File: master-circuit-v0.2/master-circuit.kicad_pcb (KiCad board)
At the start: 4 copper layers, 64 x 86 mm, 254 parts, among them U6 20nF 5%, X2 24MHz

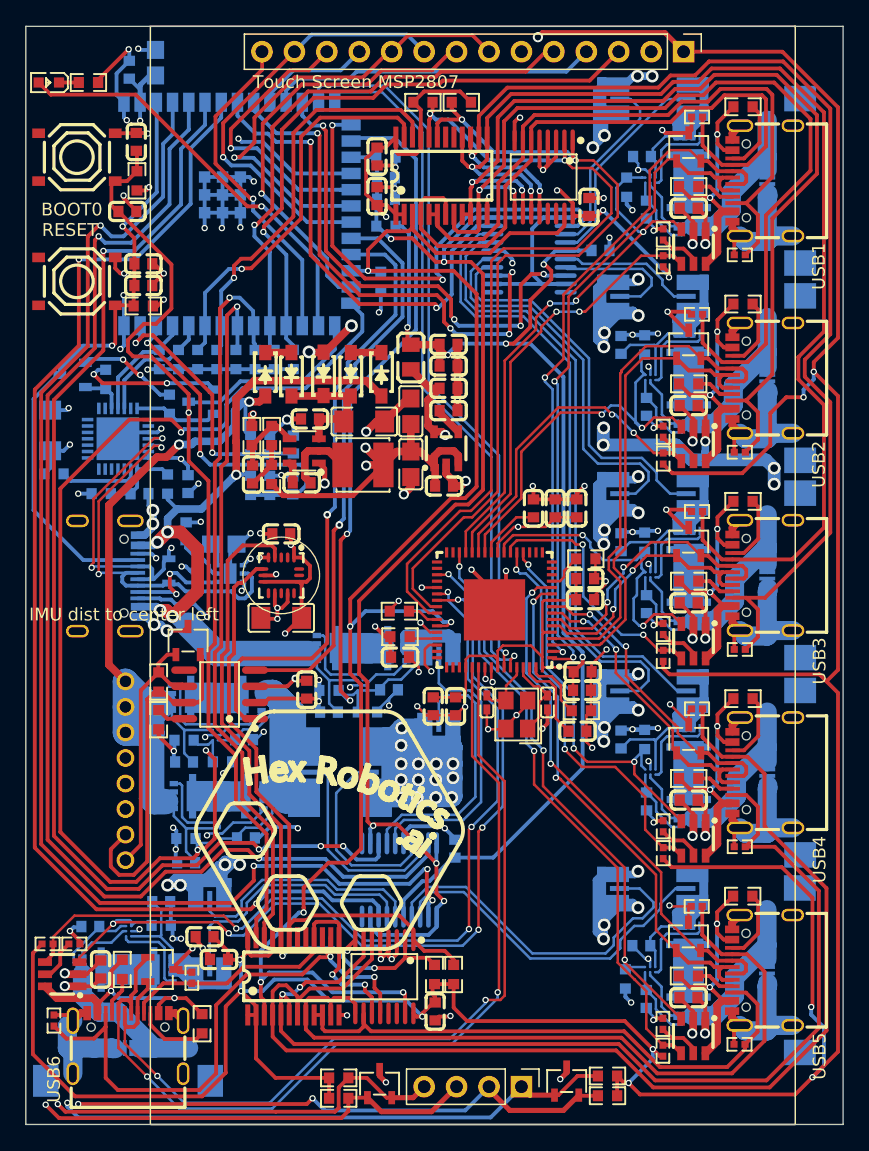
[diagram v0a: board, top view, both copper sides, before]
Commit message: Argh, some chips out of stock, got to do a slight redesign.
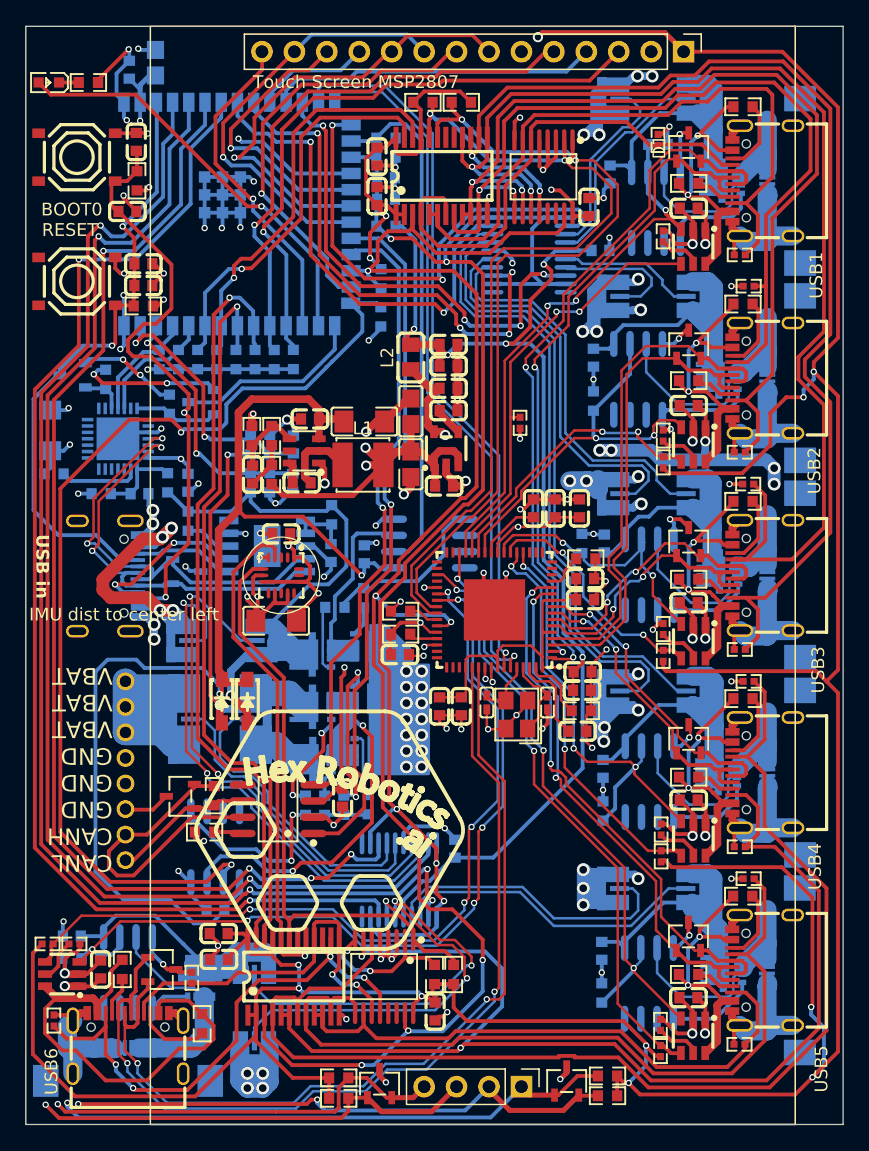
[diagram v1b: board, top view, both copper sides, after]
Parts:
- removed C14, C19, C36, C37, C46, C49, C72, C73, C74, C75, C76, C77, C78, C79, C80, C81: 1uF, Library:C0603
- removed D13, D15, D3: ~, Library:SOD-123_L2.7-W1.6-LS3.7-RD-1
- removed Q1, Q11, Q13, Q15, Q17, Q19, Q2, Q3, Q4, Q5, Q6, Q7: ~, Library:WDFN-5_L3.1-W3.1-P0.65-BL_1
- removed R19, R20, R36, R49, R54, R57, R63, R69, R75: 10kΩ, Library:R0603
- removed U12, U2, U21, U22, U25, U27, U29, U31, U8: ~, Library:WLCSP-6_L1.2-W0.8-P0.40-TL
- removed U5: ~, Library:TDFN-6_L2.0-W2.0-P0.65-TL-EP
- removed U6: 20nF 5%, Library:C0805
- added C51: 1uF, Library:C0603, B.Cu at (145.8, 68.6)
- added C52: 1uF, Library:C0603, B.Cu at (144.4, 83.0)
- added C53: 1uF, Library:C0603, B.Cu at (145.3, 97.5)
- added C54: 1uF, Library:C0603, B.Cu at (145.2, 115.2)
- added C55: 1uF, Library:C0603, B.Cu at (126.5, 98.3)
- added C56: 1uF, Library:C0603, B.Cu at (114.8, 126.2)
- added Q21: ~, Library:WDFN-5_L3.1-W3.1-P0.65-BL_1, B.Cu at (123.2, 114.4)
- added Q22: ~, Library:WDFN-5_L3.1-W3.1-P0.65-BL_1, B.Cu at (126.5, 113.8)
- added Q23: ~, Library:WDFN-5_L3.1-W3.1-P0.65-BL_1, B.Cu at (155.1, 99.7)
- added Q24: ~, Library:WDFN-5_L3.1-W3.1-P0.65-BL_1, B.Cu at (154.9, 115.5)
- added Q25: ~, Library:WDFN-5_L3.1-W3.1-P0.65-BL_1, B.Cu at (155.3, 130.9)
- added Q26: ~, Library:WDFN-5_L3.1-W3.1-P0.65-BL_1, B.Cu at (113.7, 132.2)
- added R102: 10kΩ, Library:R0603, B.Cu at (145.1, 132.7)
- added R109: 10kΩ, Library:R0603, B.Cu at (103.6, 130.0)
- added R68: 1kΩ, Library:R0603, B.Cu at (124.0, 95.2)
- added R72: 10kΩ, Library:R0603, B.Cu at (112.7, 95.8)
- added R73: 10kΩ, Library:R0603, B.Cu at (149.5, 66.2)
- added R74: 10kΩ, Library:R0603, B.Cu at (144.4, 86.3)
- added R77: 4.7Ω, Library:R0603, B.Cu at (126.5, 101.8)
- added R78: 10kΩ, Library:R0603, B.Cu at (143.6, 97.5)
- added R81: 4.7Ω, Library:R0603, B.Cu at (124.2, 102.5)
- added R90: 4.7Ω, Library:R0603, B.Cu at (121.9, 118.0)
- added R92: 4.7Ω, Library:R0603, B.Cu at (124.9, 118.0)
- added R93: 4.7Ω, Library:R0603, B.Cu at (123.4, 118.0)
- added R94: 4.7Ω, Library:R0603, B.Cu at (126.8, 118.0)
- added R95: 10kΩ, Library:R0603, B.Cu at (145.2, 118.5)
- added U41: ~, Library:SOIC-8_L4.9-W3.9-P1.27-LS6.0-BL, B.Cu at (149.3, 71.2)
- added U42: ~, Library:ESSOP-10_L4.9-W3.9-P1.0-LS6.0-TL-EP, B.Cu at (118.9, 97.7)
- added U43: ~, Library:SOIC-8_L4.9-W3.9-P1.27-LS6.0-BL, B.Cu at (147.9, 84.7)
- added U44: ~, Library:SOIC-8_L4.9-W3.9-P1.27-LS6.0-BL, B.Cu at (148.8, 100.0)
- added U45: ~, Library:SOIC-8_L4.9-W3.9-P1.27-LS6.0-BL, B.Cu at (148.8, 116.2)
- added U46: ~, Library:SOIC-8_L4.9-W3.9-P1.27-LS6.0-BL, B.Cu at (131.6, 97.5)
- added U47: ~, Library:SOIC-8_L4.9-W3.9-P1.27-LS6.0-BL, B.Cu at (114.8, 121.2)
- added U48: ~, Library:SOIC-8_L4.9-W3.9-P1.27-LS6.0-BL, B.Cu at (148.8, 131.9)
- added U49: ~, Library:SOIC-8_L4.9-W3.9-P1.27-LS6.0-BL, B.Cu at (108.0, 131.1)
- moved C58 75.6 mm to (103.6, 128.2)
- moved C57 58.2 mm to (145.1, 129.4)
- moved R12 45.0 mm to (128.2, 65.8)
- moved R11 37.0 mm to (127.8, 79.8), turned to 90 degrees
- moved Q18 33.8 mm to (123.2, 110.3), turned to -90 degrees
- moved Q14 30.1 mm to (123.2, 106.2), turned to -90 degrees
- moved D14 27.7 mm to (117.3, 109.8)
- moved Q16 26.4 mm to (126.5, 105.5), turned to 90 degrees
- moved Q20 26.4 mm to (126.5, 109.7), turned to 90 degrees
- moved D12 25.8 mm to (115.3, 109.8)
- moved R7 17.4 mm to (115.3, 105.1), turned to 0 degrees
- moved R79 16.9 mm to (138.7, 88.0)
- moved D7 12.2 mm to (112.1, 117.3), turned to 180 degrees
- moved C29 11.6 mm to (123.9, 98.2), turned to 90 degrees
- moved R8 10.3 mm to (115.2, 111.2)
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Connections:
- C21 pad 2: /Buck-VIN -> VANY
- C22 pad 2: /Buck-VIN -> VANY
- C29 pad 2: /VBUS_PROBE -> /PD-VDD
- C57 pad 2: /servo-usb-connector/VCCx -> /servo-usb-connector4/VCCx-probe
- C58 pad 2: /servo-usb-connector/back-to-back-mosfets3/VIN -> /servo-usb-connector5/VCCx-probe
- D12 pad 1: /VBATTERY_MID_DIODE -> VANY
- D14 pad 1: /VBUS_MID_DIODE -> VANY
- Q12 pad 1: /servo-usb-connector1/back-to-back-mosfets3/VIN -> /servo-usb-connector1/VCCx
- Q12 pad 2: /servo-usb-connector1/back-to-back-mosfets3/VIN -> /servo-usb-connector1/VCCx
- Q12 pad 3: /servo-usb-connector1/back-to-back-mosfets3/VIN -> /servo-usb-connector1/VCCx
- Q12 pad 4: /servo-usb-connector1/back-to-back-mosfets3/GATE1x -> Net-(Q12-G)
- Q12 pad 5: /servo-usb-connector1/back-to-back-mosfets3/Mid-MOSFETSx -> /servo-usb-connector1/VCCx-probe
- Q14 pad 1: /servo-usb-connector2/back-to-back-mosfets3/VIN -> /Source-vbus
- Q14 pad 2: /servo-usb-connector2/back-to-back-mosfets3/VIN -> /Source-vbus
- Q14 pad 3: /servo-usb-connector2/back-to-back-mosfets3/VIN -> /Source-vbus
- Q14 pad 4: /servo-usb-connector2/back-to-back-mosfets3/GATE1x -> /Gate1-vbus
- Q14 pad 5: /servo-usb-connector2/back-to-back-mosfets3/Mid-MOSFETSx -> VBUS
- Q16 pad 1: /servo-usb-connector3/back-to-back-mosfets3/VIN -> /Source-vbus
- Q16 pad 2: /servo-usb-connector3/back-to-back-mosfets3/VIN -> /Source-vbus
- Q16 pad 3: /servo-usb-connector3/back-to-back-mosfets3/VIN -> /Source-vbus
- Q16 pad 4: /servo-usb-connector3/back-to-back-mosfets3/GATE1x -> /Gate2-vbus
- Q16 pad 5: /servo-usb-connector3/back-to-back-mosfets3/Mid-MOSFETSx -> VCC
- Q18 pad 1: /servo-usb-connector4/back-to-back-mosfets3/VIN -> /Source-vbattery
- Q18 pad 2: /servo-usb-connector4/back-to-back-mosfets3/VIN -> /Source-vbattery
- Q18 pad 3: /servo-usb-connector4/back-to-back-mosfets3/VIN -> /Source-vbattery
- Q18 pad 4: /servo-usb-connector4/back-to-back-mosfets3/GATE1x -> /Gate1-vbattery
- Q18 pad 5: /servo-usb-connector4/back-to-back-mosfets3/Mid-MOSFETSx -> VBATTERY
- Q20 pad 1: /servo-usb-connector5/back-to-back-mosfets3/VIN -> /Source-vbattery
- Q20 pad 2: /servo-usb-connector5/back-to-back-mosfets3/VIN -> /Source-vbattery
- Q20 pad 3: /servo-usb-connector5/back-to-back-mosfets3/VIN -> /Source-vbattery
- Q20 pad 4: /servo-usb-connector5/back-to-back-mosfets3/GATE1x -> /Gate2-vbattery
- Q20 pad 5: /servo-usb-connector5/back-to-back-mosfets3/Mid-MOSFETSx -> VCC
- Q8 pad 1: /servo-usb-connector/back-to-back-mosfets3/VIN -> /servo-usb-connector/VCCx
- Q8 pad 2: /servo-usb-connector/back-to-back-mosfets3/VIN -> /servo-usb-connector/VCCx
- Q8 pad 3: /servo-usb-connector/back-to-back-mosfets3/VIN -> /servo-usb-connector/VCCx
- Q8 pad 4: /servo-usb-connector/back-to-back-mosfets3/GATE1x -> Net-(Q8-G)
- Q8 pad 5: /servo-usb-connector/back-to-back-mosfets3/Mid-MOSFETSx -> /servo-usb-connector/VCCx-probe
- R1 pad 1: /servo-usb-connector/back-to-back-mosfets3/VIN -> /servo-usb-connector/VCCx-probe
- R2 pad 1: /servo-usb-connector1/back-to-back-mosfets3/VIN -> /servo-usb-connector1/VCCx-probe
- R3 pad 1: /servo-usb-connector2/back-to-back-mosfets3/VIN -> /servo-usb-connector2/VCCx-probe
- R4 pad 1: /servo-usb-connector3/back-to-back-mosfets3/VIN -> /servo-usb-connector3/VCCx-probe
- R5 pad 1: /servo-usb-connector4/back-to-back-mosfets3/VIN -> /servo-usb-connector4/VCCx-probe
- R6 pad 1: /servo-usb-connector5/back-to-back-mosfets3/VIN -> /servo-usb-connector5/VCCx-probe
- R7 pad 1: /VBUS_PROBE -> VBUS_PINS
- R7 pad 2: VCC -> VBUS
- R8 pad 1: /VBATTERY_PROBE -> /VBATTERY_PINS
- R8 pad 2: VCC -> VBATTERY
- U1 pad 22: CAN_RX -> CAN_TX
- U1 pad 23: CAN_TX -> CAN_RX
- U1 pad 5: BATTERY_CURRENT -> VBUS_CURRENT
- U1 pad 6: VBUS_CURRENT -> BATTERY_CURRENT
- U16 pad 13: VBUS_CURRENT -> BATTERY_CURRENT
- U16 pad 14: +Probe-7 -> +Probe-8
- U16 pad 15: -Probe-7 -> -Probe-8
- U16 pad 17: +Probe-8 -> +Probe-7
- U16 pad 18: -Probe-8 -> -Probe-7
- U16 pad 19: BATTERY_CURRENT -> VBUS_CURRENT
- U16 pad 6: +Probe-6 -> -Probe-6
- U16 pad 7: -Probe-6 -> +Probe-6
- U19 pad 6: VBATTERY -> /VBATTERY_PINS
- U19 pad 7: VBATTERY -> /VBATTERY_PINS
- U19 pad 8: VBATTERY -> /VBATTERY_PINS
- U4 pad 3: /Buck-VIN -> VANY
- USB0 pad A4B9: VBUS -> VBUS_PINS
- USB0 pad B4A9: VBUS -> VBUS_PINS
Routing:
- net VCC: track 191.1 -> 88.7 mm, vias 40 -> 38
- net VANY: track 0.00 -> 93.9 mm, vias 0 -> 2
- net VBATTERY: track 69.7 -> 35.4 mm
- net /Source-vbattery: track 0.00 -> 31.7 mm, vias 0 -> 2
- net /VBATTERY_PROBE: track 30.3 -> 0.00 mm
- net VBUS: track 70.7 -> 46.3 mm, vias 5 -> 1
- net VBUS_PINS: track 0.00 -> 23.8 mm, vias 0 -> 4
- net /servo-usb-connector5/VCCx-probe: track 0.00 -> 23.0 mm
- net /servo-usb-connector3/back-to-back-mosfets3/VIN: track 22.0 -> 0.00 mm
- net /servo-usb-connector1/back-to-back-mosfets3/VIN: track 22.0 -> 0.00 mm
- net /servo-usb-connector2/back-to-back-mosfets3/VIN: track 22.0 -> 0.00 mm
- net /servo-usb-connector5/back-to-back-mosfets3/VIN: track 22.0 -> 0.00 mm
- net /servo-usb-connector4/VCCx-probe: track 0.00 -> 21.3 mm
- net /servo-usb-connector/VCCx-probe: track 0.00 -> 20.9 mm
- net +Probe-7: track 21.3 -> 42.0 mm, vias 0 -> 2
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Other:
- board text added: "VCC | GND"
- board text removed: "VCC|GND"
